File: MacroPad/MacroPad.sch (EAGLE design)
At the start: 69 parts, among them IC1 MIC5219BM5, J1 USB4085-GF-A_REVA4, U1 ATMEGA32U4-AUR, Y1 XRCGB16M000FXN00R0

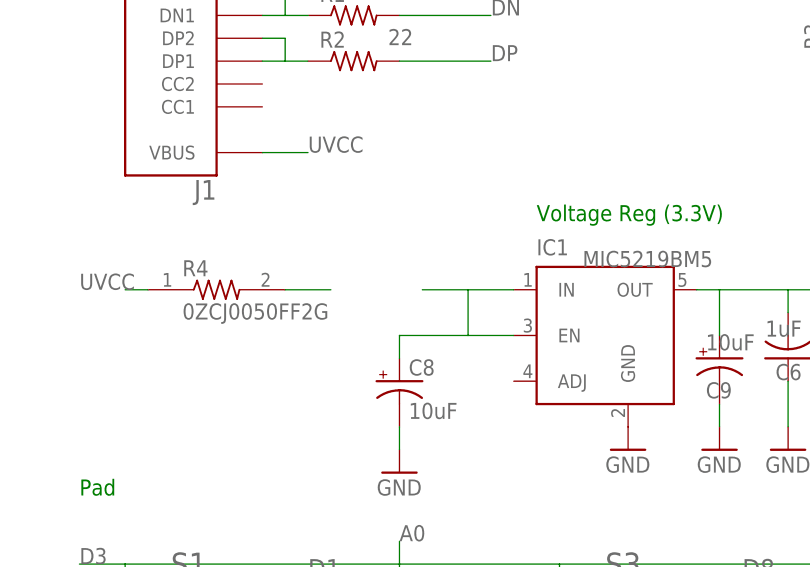
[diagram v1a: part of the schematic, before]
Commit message: Added missing diode
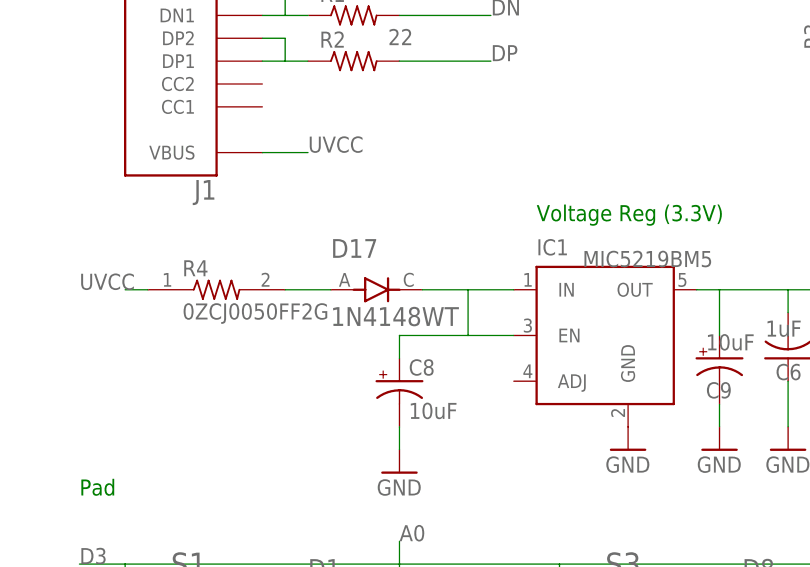
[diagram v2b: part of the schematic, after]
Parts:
- added D17: 1N4148WT, 1N4148WT:1N4148WT
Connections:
- net N$17: now also D17.A
- net N$25: now also D17.C
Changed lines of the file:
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@@
 <part name="D16" library="1N4148WT" deviceset="1N4148WT" device=""/>
 <part name="J1" library="USB4085-GF-A_REVA4" deviceset="USB4085-GF-A_REVA4" device=""/>
+<part name="D17" library="1N4148WT" deviceset="1N4148WT" device=""/>
 </parts>
 <sheets>
@@
 <attribute name="NAME" x="83.82" y="108.712" size="2.1844" layer="95" rot="R180"/>
 <attribute name="VALUE" x="83.82" y="147.32" size="2.1844" layer="96" rot="R180"/>
+</instance>
+<instance part="D17" gate="G$1" x="101.6" y="96.52" smashed="yes">
+<attribute name="NAME" x="96.51298125" y="100.06481875" size="2.08563125" layer="95" ratio="10" rot="SR0"/>
+<attribute name="VALUE" x="96.48326875" y="92.49985" size="2.088559375" layer="96" ratio="10" rot="SR0"/>
 </instance>
 </instances>
@@
 <pinref part="C8" gate="G$1" pin="+"/>
 <wire x1="106.68" y1="96.52" x2="111.76" y2="96.52" width="0.1524" layer="91"/>
+<pinref part="D17" gate="G$1" pin="C"/>
 </segment>
 </net>
@@
 <pinref part="R4" gate="G$1" pin="2"/>
 <wire x1="91.44" y1="96.52" x2="96.52" y2="96.52" width="0.1524" layer="91"/>
-</segment>
-</net>
+<pinref part="D17" gate="G$1" pin="A"/>
+</segment>
+</net>

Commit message: Further board errors corrected, BOM included
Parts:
- removed SG1: EFBAA40D101, buzzer:EFBAA40D101
- added U$17: PT-1307, PT-1307:PT-1307
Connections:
- net D7: now also U$17.P$2; no longer SG1.2
- net DGND: now also U$17.P$1; no longer SG1.1
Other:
- moved on the sheet: C1, C2, C3, C4, C5, C6, C7, C8, C9, D1, D10, D11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
